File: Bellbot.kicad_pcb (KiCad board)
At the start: 4 copper layers, 150 x 144 mm, 132 parts, among them J1 Conn_01x02, J10 Conn_01x03, J11 Conn_01x03, J12 Conn_01x03, J13 Conn_01x03, J14 Conn_01x08, J15 Conn_01x12, J2 Conn_01x04, J3 Conn_01x06, J4 Conn_01x06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

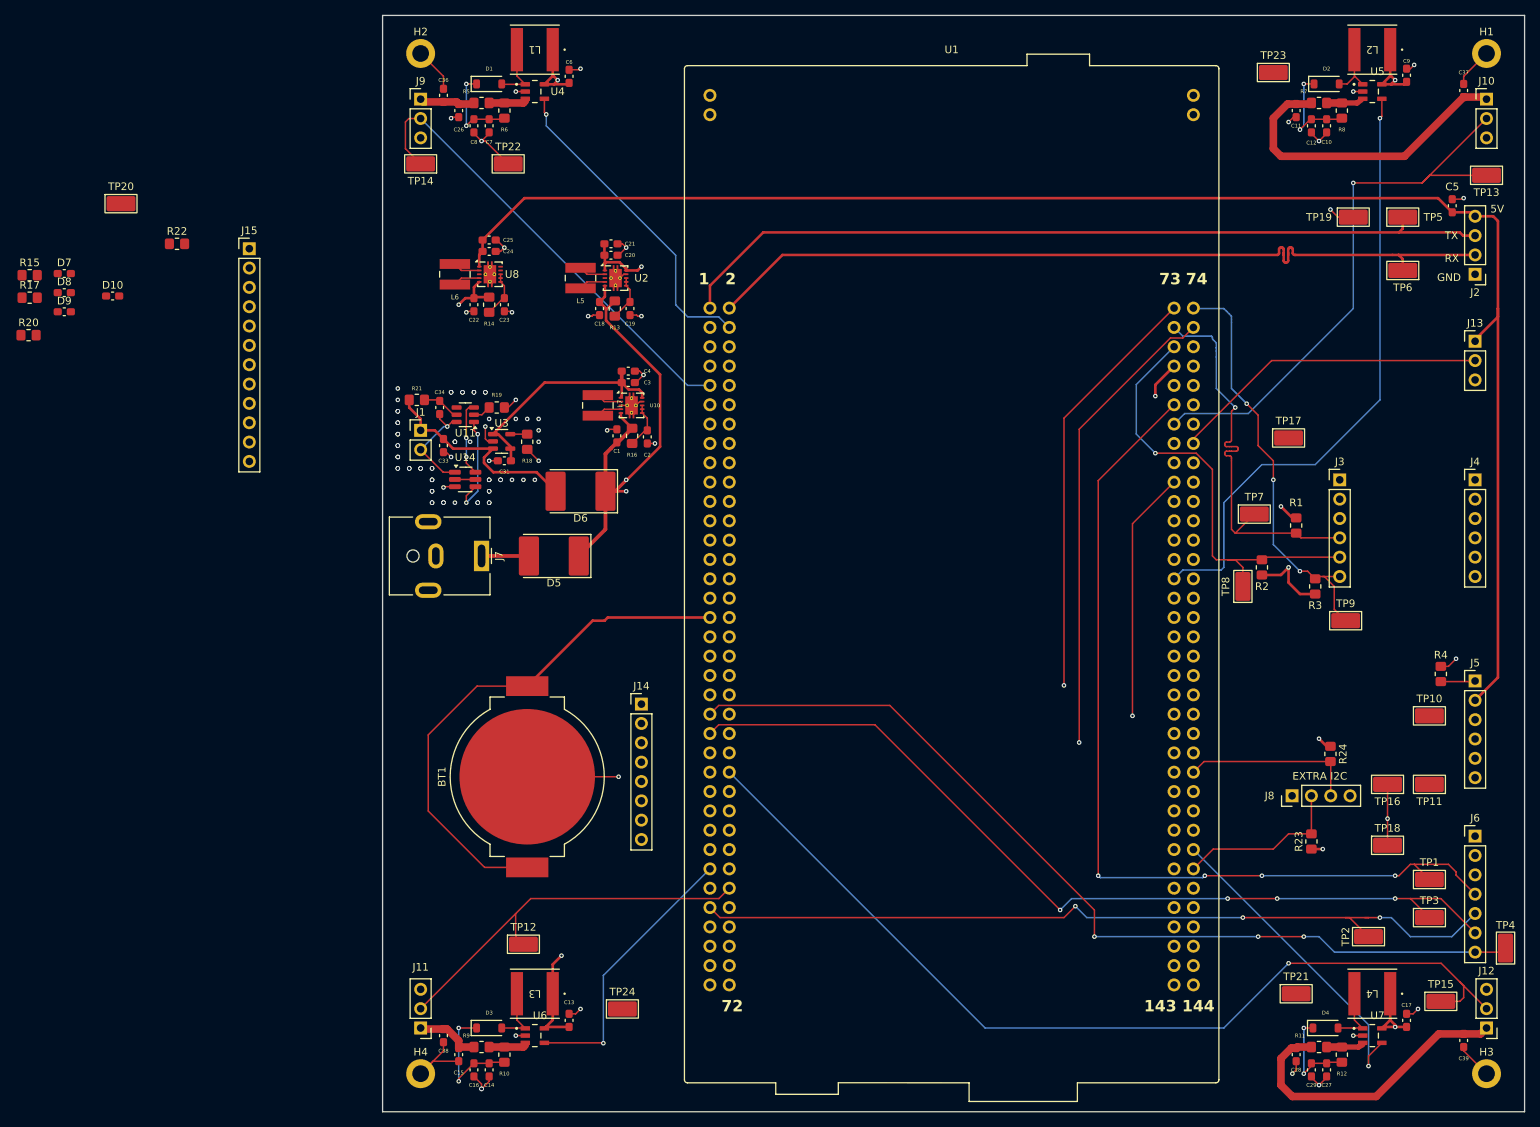
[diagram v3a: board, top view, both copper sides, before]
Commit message: routed quad spi
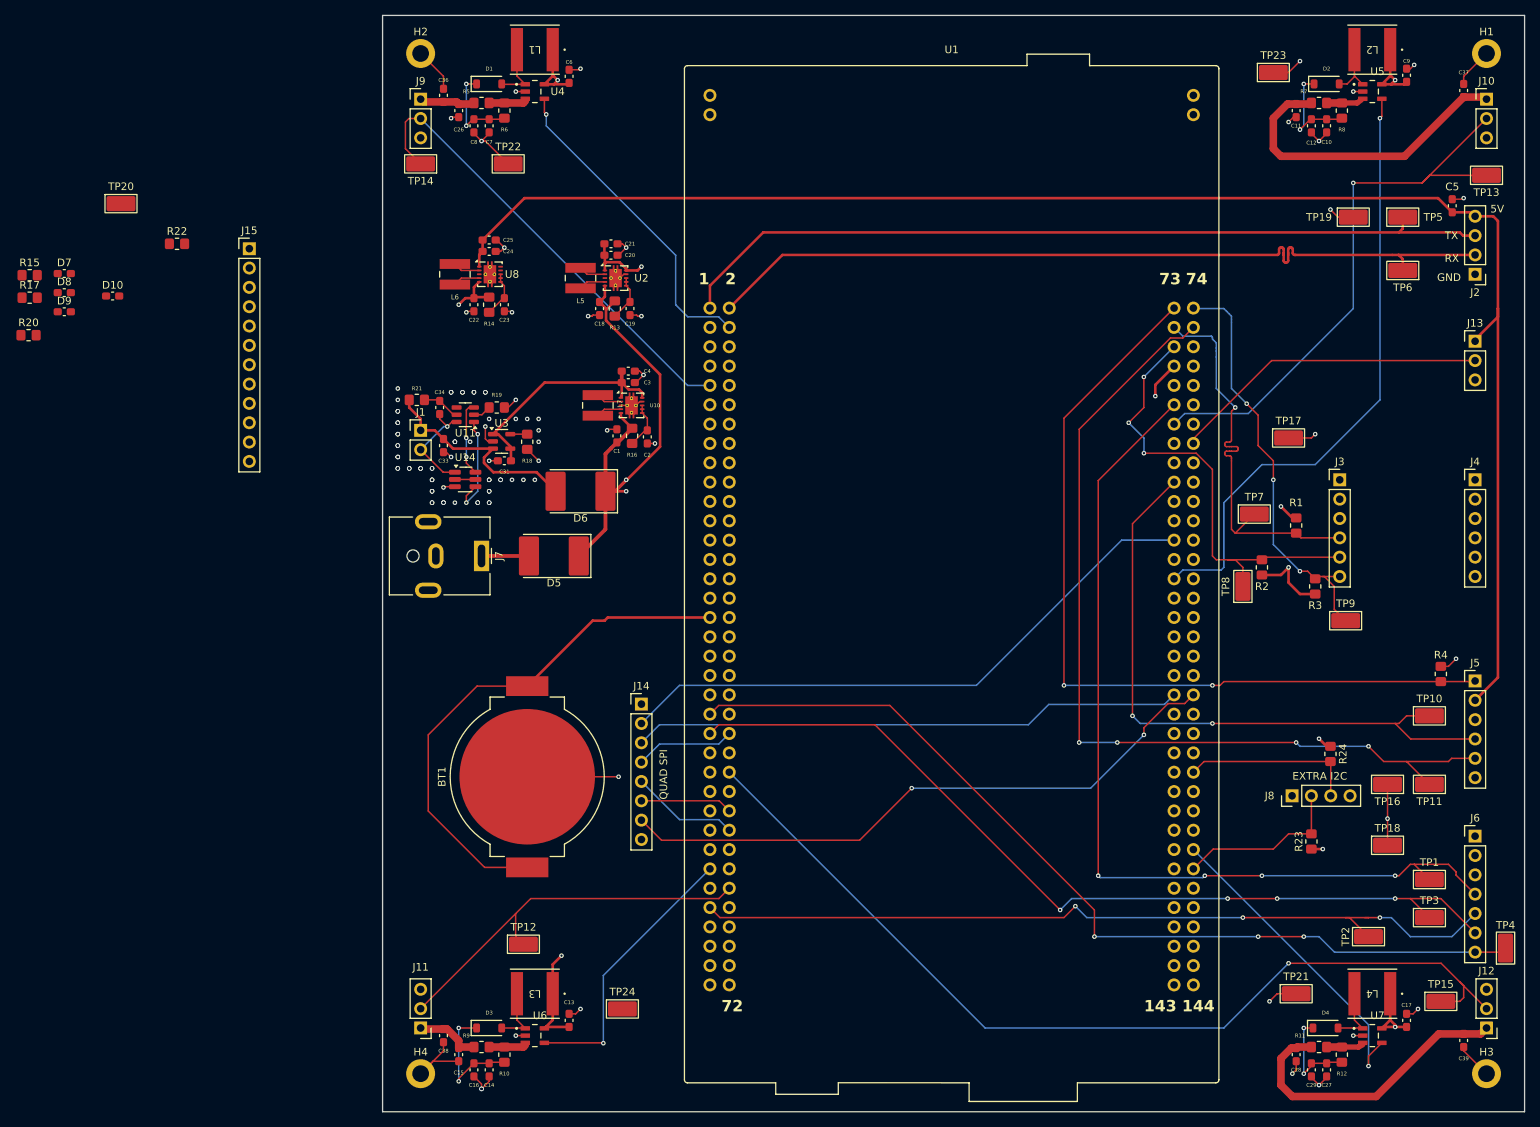
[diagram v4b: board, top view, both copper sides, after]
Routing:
- net QUADSPI_CLK: track 0.00 -> 82.1 mm, vias 0 -> 2
- net QUADSPI_NCS: track 0.00 -> 79.9 mm
- net QUADSPI_IO3: track 0.00 -> 72.6 mm
- net HC05_TX: track 61.7 -> 119.1 mm, vias 1 -> 4
- net HC05_RX: track 33.0 -> 84.1 mm, vias 1 -> 2
- net HC-05_MODE: track 60.1 -> 109.8 mm, vias 1 -> 2
- net QUADSPI_IO1: track 0.00 -> 14.2 mm
- net QUADSPI_IO2: track 0.00 -> 13.1 mm
- net QUADSPI_IO0: track 0.00 -> 12.1 mm
- net GND: track 117.8 -> 129.5 mm, vias 95 -> 98
- net I2C_SDA: track 58.8 -> 60.5 mm, vias 1 -> 3
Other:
- board text added: "QUAD SPI"
